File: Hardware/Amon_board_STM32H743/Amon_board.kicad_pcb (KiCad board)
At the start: 4 copper layers, 70 x 120 mm, 132 parts, among them J1 USB2.0_C_Rev, J10 GTFP08131Y2HR, J11 Conn_01x03_Male, J12 Conn_01x06_Male, J13 Conn_01x04_Male, J14 Conn_01x04_Male, J15 Conn_01x06_Male, J2 Conn_2x5 pin, J3 Switch_port, J4 XT60-F, J5 XT60-F, J6 Conn_02x04_Odd_Even, J7 Red leds, J8 White leds, J9 Conn_02x04_Odd_Even, M1 Servo_X+, M2 Servo_X-, M3 Servo_Y+, M4 Servo_Y-, Q1 BC817, Q2 BC817, SW1 SW_DPDT, SW2 SW_SPST, U1 USBLC6-2P6, U2 STM32F405RGT6-LQFP64, U3 W25Q128JVS, U4 MP2303ADN, U5 MP2303ADN, U6 MPU-6050, U7 BME280, U8 HMC5883L, Y1 25MHz

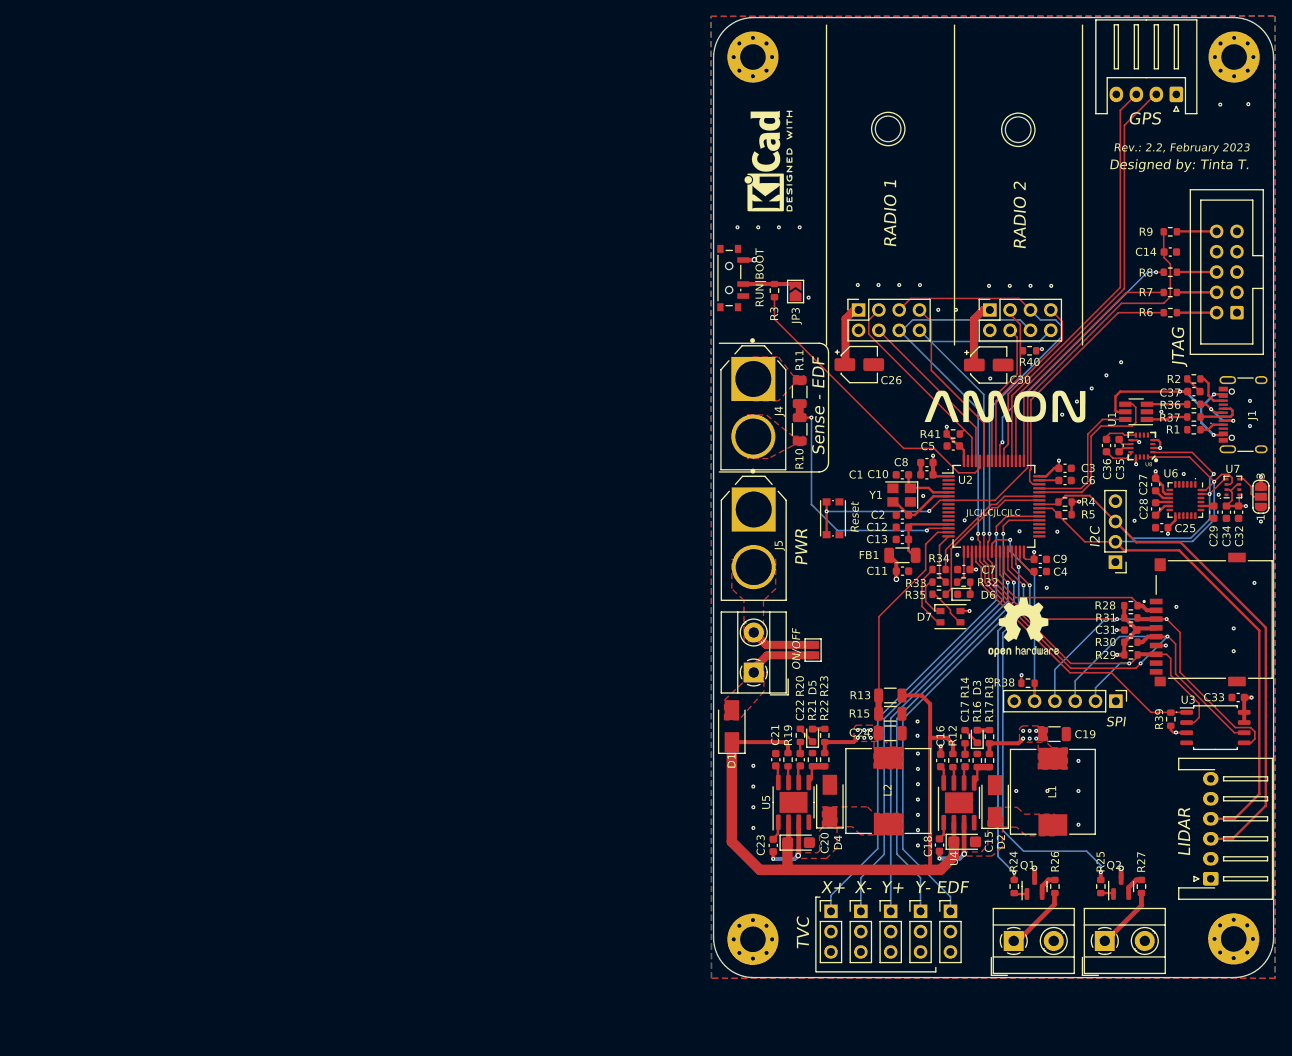
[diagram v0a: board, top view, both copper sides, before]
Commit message: Update
compas driver - untested
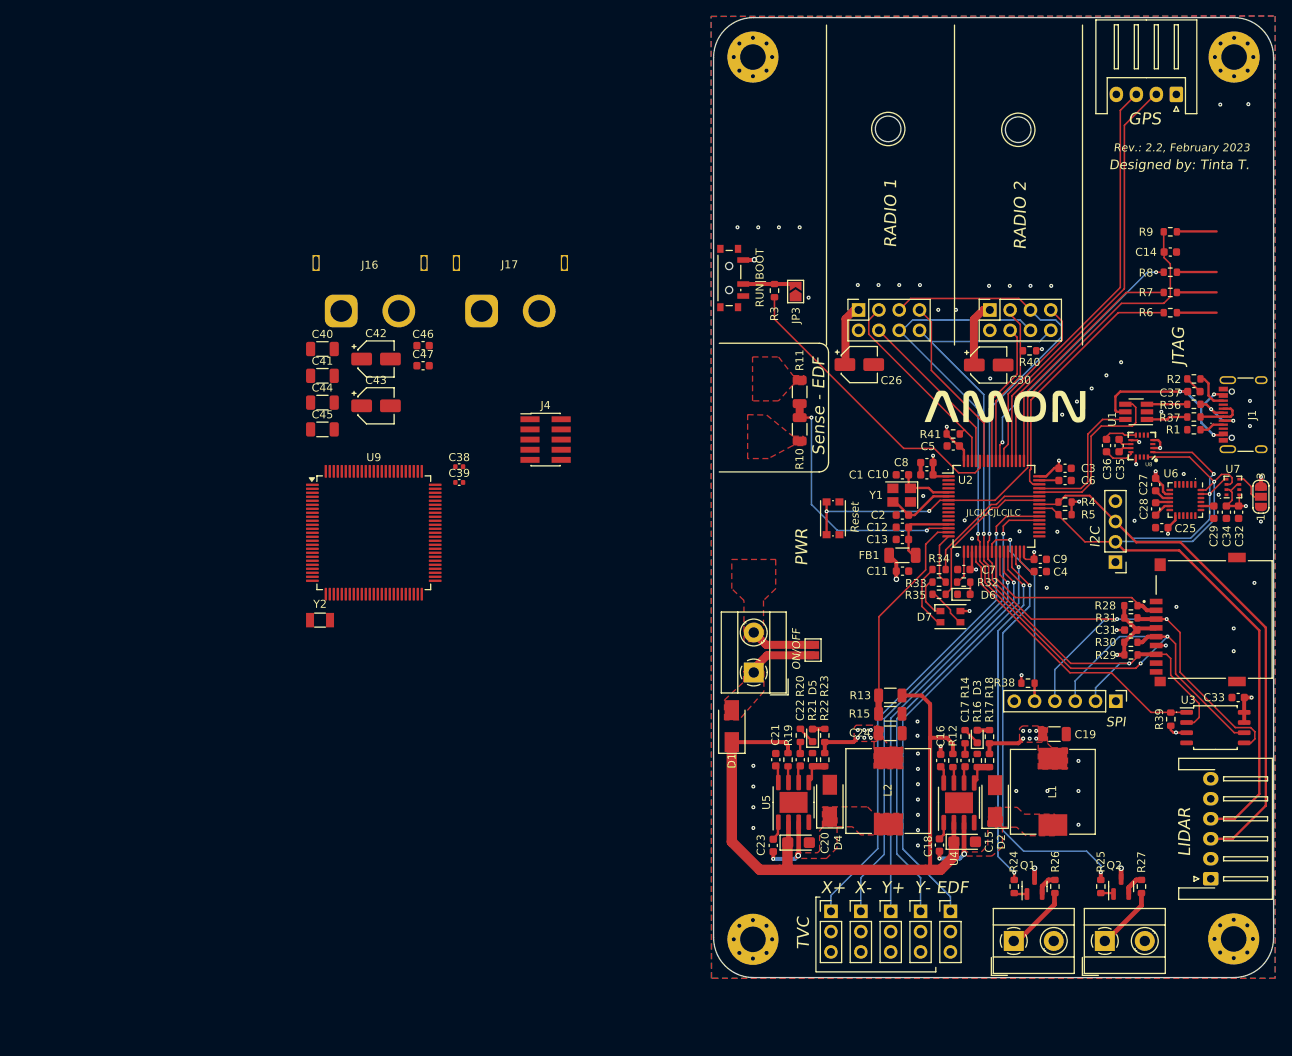
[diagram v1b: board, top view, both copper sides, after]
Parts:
- removed J2: Conn_2x5 pin, Connector_IDC:IDC-Header_2x05_P2.54mm_Vertical
- removed J5: XT60-F, XT60:AMASS_XT60-M
- removed REF**: OSHW-Logo2_9.8x8mm_SilkScreen, Symbol:OSHW-Logo2_9.8x8mm_SilkScreen
- removed REF**: KiCad-Logo2_5mm_SilkScreen, Symbol:KiCad-Logo2_5mm_SilkScreen
- added C38: 22pF, Capacitor_SMD:C_0402_1005Metric, F.Cu at (123.2, 85.1)
- added C39: 22pF, Capacitor_SMD:C_0402_1005Metric, F.Cu at (123.2, 87.1)
- added C40: 22uF, Capacitor_SMD:C_1206_3216Metric, F.Cu at (106.1, 70.4)
- added C41: 22uF, Capacitor_SMD:C_1206_3216Metric, F.Cu at (106.1, 73.8)
- added C42: 10uF, Capacitor_SMD:CP_Elec_4x5.4, F.Cu at (112.8, 71.7)
- added C43: 10uF, Capacitor_SMD:CP_Elec_4x5.4, F.Cu at (112.8, 77.5)
- added C44: 22uF, Capacitor_SMD:C_1206_3216Metric, F.Cu at (106.1, 77.1)
- added C45: 22uF, Capacitor_SMD:C_1206_3216Metric, F.Cu at (106.1, 80.5)
- added C46: 100nF, Capacitor_SMD:C_0603_1608Metric, F.Cu at (118.7, 70.0)
- added C47: 100nF, Capacitor_SMD:C_0603_1608Metric, F.Cu at (118.7, 72.5)
- added J16: XT60PW-M20, Connector_AMASS:AMASS_XT60PW-M_1x02_P7.20mm_Horizontal, F.Cu at (108.5, 65.7)
- added J17: XT60PW-M20, Connector_AMASS:AMASS_XT60PW-M_1x02_P7.20mm_Horizontal, F.Cu at (126.0, 65.7)
- added U9: STM32H743VIT6, Package_QFP:LQFP-100_14x14mm_P0.5mm, F.Cu at (112.5, 93.4)
- added Y2: 32.768kHz, Crystal:Crystal_SMD_3215-2Pin_3.2x1.5mm, F.Cu at (105.8, 104.3)
- C1, C2: value 14pF -> 15pF
- J4: value XT60-F -> HAB-VCR-010-LF; footprint XT60:AMASS_XT60-M -> Connector_PinHeader_1.27mm:PinHeader_2x05_P1.27mm_Vertical_SMD
- Y1: value 25MHz -> 48MHz
- moved J4 26.3 mm to (134.0, 81.8), turned to 0 degrees
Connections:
- C1 pad 1: /HSE_IN -> /Microcontroller/HSE_IN
- C14 pad 1: /NRST -> /Microcontroller/NRST
- C2 pad 1: /HSE_OUT -> /Microcontroller/HSE_OUT
- J4 pad 1: GND1 -> +3V3
- J4 pad 2: Net-(J4-+) -> Net-(J4-Pin_2)
- R10 pad 1: Net-(J4-+) -> Net-(J17-Pin_2)
- R11 pad 2: GND1 -> GND
- R6 pad 1: Net-(J2-Pin_2) -> Net-(J4-Pin_2)
- R6 pad 2: /SWDIO -> /Microcontroller/SWDIO
- R7 pad 1: Net-(J2-Pin_4) -> Net-(J4-Pin_4)
- R7 pad 2: /SWDCLK -> /Microcontroller/SWDCLK
- R8 pad 1: Net-(J2-Pin_6) -> Net-(J4-Pin_6)
- R8 pad 2: /SWO -> /Microcontroller/SWO
- R9 pad 1: Net-(J2-Pin_10) -> Net-(J4-Pin_10)
- R9 pad 2: /NRST -> /Microcontroller/NRST
- Y1 pad 1: /HSE_IN -> /Microcontroller/HSE_IN
- Y1 pad 3: /HSE_OUT -> /Microcontroller/HSE_OUT
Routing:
- net Net-(J4-Pin_10): track 0.00 -> 4.99 mm
- net Net-(J2-Pin_10): track 4.99 -> 0.00 mm
- net Net-(J4-Pin_6): track 0.00 -> 4.98 mm
- net Net-(J2-Pin_6): track 4.98 -> 0.00 mm
- net Net-(J4-Pin_4): track 0.00 -> 4.97 mm
- net Net-(J2-Pin_4): track 4.97 -> 0.00 mm
- net Net-(J4-Pin_2): track 0.00 -> 4.97 mm
- net Net-(J2-Pin_2): track 4.97 -> 0.00 mm
- added copper zone on F.Cu, net Net-(J17-Pin_2)
- removed copper zone on F.Cu, net GND1
- removed copper zone on F.Cu, net Net-(J4-+)

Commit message: Update: development of new PCB_v3
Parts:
- removed C1, C2: 15pF, Capacitor_SMD:C_0603_1608Metric
- removed C4, C6: 2.2uF, Capacitor_SMD:C_0603_1608Metric
- removed D1: B120-E3, Diode_SMD:D_SMA
- removed H5, H6: MountingHole, MountingHole:MountingHole_3.2mm_M3
- removed J12: Conn_01x06_Male, Connector_JST:JST_XH_S6B-XH-A-1_1x06_P2.50mm_Horizontal
- removed J6: Conn_02x04_Odd_Even, Connector_PinSocket_2.54mm:PinSocket_2x04_P2.54mm_Vertical
- removed JP3: SolderJumper_2_Open, Jumper:SolderJumper-2_P1.3mm_Open_TrianglePad1.0x1.5mm
- removed R1, R2: 5k1, Resistor_SMD:R_0603_1608Metric
- removed R3: 10k, Resistor_SMD:R_0603_1608Metric
- removed SW1: SW_DPDT, Button_Switch_SMD:SW_SPDT_PCM12
- removed SW2: SW_SPST, Button_Switch_SMD:SW_Push_1P1T_NO_CK_KMR2
- removed U1: USBLC6-2P6, Package_TO_SOT_SMD:SOT-23-6_Handsoldering
- removed U2: STM32F405RGT6-LQFP64, Package_QFP:LQFP-64_10x10mm_P0.5mm
- added C100: 100nF, Capacitor_SMD:C_0603_1608Metric, F.Cu at (104.2, 103.8)
- added C101: 10uF, Capacitor_SMD:C_1206_3216Metric, F.Cu at (115.2, 122.3)
- added C102: 10uF, Capacitor_SMD:C_1206_3216Metric, F.Cu at (98.3, 119.7)
- added C103: 10uF, Capacitor_SMD:C_1206_3216Metric, F.Cu at (80.8, 121.8)
- added C104: 10uF, Capacitor_SMD:C_1206_3216Metric, F.Cu at (80.8, 119.4)
- added C105: 10uF, Capacitor_SMD:C_1206_3216Metric, F.Cu at (80.8, 117.0)
- added C106: 10uF, Capacitor_SMD:C_1206_3216Metric, F.Cu at (98.3, 122.1)
- added C107: 10uF, Capacitor_SMD:C_1206_3216Metric, F.Cu at (98.3, 117.3)
- added C108: 10uF, Capacitor_SMD:C_1206_3216Metric, F.Cu at (115.2, 119.9)
- added C109: 10uF, Capacitor_SMD:C_1206_3216Metric, F.Cu at (115.2, 117.5)
- added C110: 4.7uF, Capacitor_SMD:C_0603_1608Metric, F.Cu at (104.2, 79.5)
- added C111: 4.7uF, Capacitor_SMD:C_0603_1608Metric, F.Cu at (117.2, 92.5)
- added C48: 0.1uF, Capacitor_SMD:C_0603_1608Metric, F.Cu at (121.5, 77.2)
- added C49: 0.1uF, Capacitor_SMD:C_0603_1608Metric, F.Cu at (125.4, 81.9)
- added C50: 10nF, Capacitor_SMD:C_0402_1005Metric, F.Cu at (102.3, 61.2)
- added C51: 10nF, Capacitor_SMD:C_0402_1005Metric, F.Cu at (82.5, 61.2)
- added C52: 33nF, Capacitor_SMD:C_0402_1005Metric, F.Cu at (102.8, 62.9)
- added C53: 33nF, Capacitor_SMD:C_0402_1005Metric, F.Cu at (83.0, 62.9)
- added C54: 1nF, Capacitor_SMD:C_0402_1005Metric, F.Cu at (110.8, 63.0)
- added C55: 1nF, Capacitor_SMD:C_0402_1005Metric, F.Cu at (91.0, 63.0)
- added C56: 1uF, Capacitor_SMD:C_0402_1005Metric, F.Cu at (104.5, 57.8)
- added C57: 1uF, Capacitor_SMD:C_0402_1005Metric, F.Cu at (84.7, 57.8)
- added C58: 22pF, Capacitor_SMD:C_0402_1005Metric, F.Cu at (112.7, 63.0)
- added C59: 22pF, Capacitor_SMD:C_0402_1005Metric, F.Cu at (92.8, 63.0)
- added C60: 22pF, Capacitor_SMD:C_0402_1005Metric, F.Cu at (111.1, 57.8)
- added C61: 22pF, Capacitor_SMD:C_0402_1005Metric, F.Cu at (91.2, 57.7)
- added C62: 2.2nF, Capacitor_SMD:C_0402_1005Metric, F.Cu at (108.4, 55.9)
- added C63: 1.5pF, Capacitor_SMD:C_0402_1005Metric, F.Cu at (106.0, 54.5)
- added C64: 2.2nF, Capacitor_SMD:C_0402_1005Metric, F.Cu at (88.5, 56.8)
- added C65: 1.5pF, Capacitor_SMD:C_0402_1005Metric, F.Cu at (86.0, 54.5)
- added C66: 1pF, Capacitor_SMD:C_0402_1005Metric, F.Cu at (105.5, 53.1)
- added C67: 1pF, Capacitor_SMD:C_0402_1005Metric, F.Cu at (85.5, 53.0)
- added C68: 4.7pF, Capacitor_SMD:C_0402_1005Metric, F.Cu at (108.4, 56.9)
- added C69: 4.7pF, Capacitor_SMD:C_0402_1005Metric, F.Cu at (88.5, 55.8)
- added C70: 220pF, Capacitor_SMD:C_0402_1005Metric, F.Cu at (102.2, 51.2)
- added C71: 220pF, Capacitor_SMD:C_0402_1005Metric, F.Cu at (82.2, 51.2)
- added C72: 0.3pF, Capacitor_SMD:C_0402_1005Metric, F.Cu at (106.0, 47.7)
- added C73: 0.3pF, Capacitor_SMD:C_0402_1005Metric, F.Cu at (86.0, 47.7)
- added C74: 1uF, Capacitor_SMD:C_0402_1005Metric, F.Cu at (102.2, 52.2)
- added C75: 1uF, Capacitor_SMD:C_0402_1005Metric, F.Cu at (82.2, 52.2)
- added C76: 1.5pF, Capacitor_SMD:C_0402_1005Metric, F.Cu at (106.0, 46.7)
- added C77: 1.5pF, Capacitor_SMD:C_0402_1005Metric, F.Cu at (86.0, 46.7)
- added C78: 1.5pF, Capacitor_SMD:C_0402_1005Metric, F.Cu at (106.0, 43.9)
- added C79: 1.5pF, Capacitor_SMD:C_0402_1005Metric, F.Cu at (86.0, 43.9)
- added C80: 1uF, Capacitor_SMD:C_0603_1608Metric, F.Cu at (128.7, 129.2)
- added C81: 1uF, Capacitor_SMD:C_0603_1608Metric, F.Cu at (127.9, 145.2)
- added C82: 0.1uF, Capacitor_SMD:C_0603_1608Metric, F.Cu at (92.1, 107.5)
- added C83: 1uF, Capacitor_SMD:C_0603_1608Metric, F.Cu at (98.3, 106.5)
- added C84: 100nF, Capacitor_SMD:C_0603_1608Metric, F.Cu at (99.3, 105.4)
- added C85: 10nF, Capacitor_SMD:C_0603_1608Metric, F.Cu at (122.0, 71.5)
- added C86: 22pF, Capacitor_SMD:C_0402_1005Metric, F.Cu at (127.4, 70.9)
- added C87: 10uF, Capacitor_Tantalum_SMD:CP_EIA-3216-10_Kemet-I, F.Cu at (122.5, 136.5)
- added C88: 100nF, Capacitor_SMD:C_0603_1608Metric, F.Cu at (112.4, 139.3)
- added C89: 3.9nF, Capacitor_SMD:C_0603_1608Metric, F.Cu at (112.4, 136.2)
- added C90: 10nF, Capacitor_SMD:C_0603_1608Metric, F.Cu at (123.0, 139.6)
- added C91: 22uF, Capacitor_SMD:C_1206_3216Metric, F.Cu at (112.0, 130.0)
- added C92: 22pF, Capacitor_SMD:C_0402_1005Metric, F.Cu at (96.6, 103.3)
- added C93: 22uF, Capacitor_SMD:C_1206_3216Metric, F.Cu at (119.9, 122.3)
- added C94: 22uF, Capacitor_SMD:C_1206_3216Metric, F.Cu at (119.9, 119.9)
- added C95: 100nF, Capacitor_SMD:C_0603_1608Metric, F.Cu at (119.2, 117.5)
- added C96: 100nF, Capacitor_SMD:C_0603_1608Metric, F.Cu at (102.3, 117.3)
- added C97: 100nF, Capacitor_SMD:C_0603_1608Metric, F.Cu at (84.8, 117.0)
- added C98: 100nF, Capacitor_SMD:C_0603_1608Metric, F.Cu at (91.9, 127.1)
- added C99: 100nF, Capacitor_SMD:C_0603_1608Metric, F.Cu at (108.8, 126.9)
- added D10: Red, LED_SMD:LED_0603_1608Metric, F.Cu at (109.3, 134.7)
- added D8: B120-E3, Diode_SMD:D_SMA, F.Cu at (83.4, 110.4)
- added D9: B120-E3, Diode_SMD:D_SMA, F.Cu at (117.6, 132.6)
- added J18: SMA Edge, Connector_Coaxial:SMA_Amphenol_132289_EdgeMount, F.Cu at (105.6, 39.5)
- added J19: SMA Edge, Connector_Coaxial:SMA_Amphenol_132289_EdgeMount, F.Cu at (85.6, 39.5)
- added J2: Conn_01x04_Pin, Connector_JST:JST_EH_S4B-EH_1x04_P2.50mm_Horizontal, F.Cu at (131.0, 137.0)
- added J5: Conn_01x04_Pin, Connector_JST:JST_EH_S4B-EH_1x04_P2.50mm_Horizontal, F.Cu at (131.0, 109.5)
- added L10: 2.4nH, Inductor_SMD:L_0402_1005Metric, F.Cu at (85.5, 45.3)
- added L11: 10uH 4A, Inductor_SMD:L_APV_APH0630, F.Cu at (117.7, 127.1)
- added L3: 8.2nH, Inductor_SMD:L_0402_1005Metric, F.Cu at (106.5, 57.8)
- added L4: 2.7nH, Inductor_SMD:L_0402_1005Metric, F.Cu at (107.0, 56.4)
- added L5: 3.9nH, Inductor_SMD:L_0402_1005Metric, F.Cu at (106.0, 56.4)
- added L6: 8.2nH, Inductor_SMD:L_0402_1005Metric, F.Cu at (86.5, 57.8)
- added L7: 2.7nH, Inductor_SMD:L_0402_1005Metric, F.Cu at (87.0, 56.3)
- added L8: 3.9nH, Inductor_SMD:L_0402_1005Metric, F.Cu at (86.0, 56.3)
- added L9: 2.4nH, Inductor_SMD:L_0402_1005Metric, F.Cu at (105.6, 45.3)
- added Q3: BC817, Package_TO_SOT_SMD:SOT-23, F.Cu at (124.2, 146.6)
- added Q6: BC817, Package_TO_SOT_SMD:SOT-23, F.Cu at (116.7, 141.8)
- added Q7: AO3401A, Package_TO_SOT_SMD:SOT-23, F.Cu at (109.7, 141.8)
- added Q8: BC817, Package_TO_SOT_SMD:SOT-23, F.Cu at (99.6, 141.5)
- added Q9: AO3401A, Package_TO_SOT_SMD:SOT-23, F.Cu at (92.6, 141.5)
- added R42: 22k, Resistor_SMD:R_0402_1005Metric, F.Cu at (102.3, 60.0)
- added R43: 22k, Resistor_SMD:R_0402_1005Metric, F.Cu at (82.5, 60.0)
- added R44: 1M, Resistor_SMD:R_0402_1005Metric, F.Cu at (109.4, 60.4)
- added R45: 1M, Resistor_SMD:R_0402_1005Metric, F.Cu at (89.5, 60.4)
- added R46: 1k, Resistor_SMD:R_0402_1005Metric, F.Cu at (108.6, 51.7)
- added R47: 1k, Resistor_SMD:R_0402_1005Metric, F.Cu at (88.5, 51.6)
- added R48: 1k, Resistor_SMD:R_0402_1005Metric, F.Cu at (108.6, 50.7)
- added R49: 20k, Resistor_SMD:R_0402_1005Metric, F.Cu at (108.6, 49.6)
- added R50: 1k, Resistor_SMD:R_0402_1005Metric, F.Cu at (88.5, 50.6)
- added R51: 20k, Resistor_SMD:R_0402_1005Metric, F.Cu at (88.5, 49.6)
- added R52: 10k, Resistor_SMD:R_0603_1608Metric, F.Cu at (93.8, 86.4)
- added R53: 5k1, Resistor_SMD:R_0603_1608Metric, F.Cu at (129.2, 63.2)
- added R54: 100k, Resistor_SMD:R_0603_1608Metric, F.Cu at (112.4, 137.8)
- added R55: 6k8, Resistor_SMD:R_0603_1608Metric, F.Cu at (109.3, 136.2)
- added R56: 10k, Resistor_SMD:R_0603_1608Metric, F.Cu at (112.4, 134.7)
- added R57: 68k, Resistor_SMD:R_0603_1608Metric, F.Cu at (112.4, 133.1)
- added R58: 1k5, Resistor_SMD:R_0603_1608Metric, F.Cu at (109.3, 133.1)
- added R59: 1k, Resistor_SMD:R_0603_1608Metric, F.Cu at (120.7, 145.7)
- added R60: 1k, Resistor_SMD:R_0603_1608Metric, F.Cu at (120.6, 147.6)
- added R63: 10k, Resistor_SMD:R_0603_1608Metric, F.Cu at (120.3, 141.1)
- added R64: 1k, Resistor_SMD:R_0603_1608Metric, F.Cu at (120.3, 142.8)
- added R65: 10k, Resistor_SMD:R_0603_1608Metric, F.Cu at (113.3, 142.8)
- added R66: 1k, Resistor_SMD:R_0603_1608Metric, F.Cu at (113.2, 141.1)
- added R67: 10k, Resistor_SMD:R_0603_1608Metric, F.Cu at (103.1, 140.8)
- added R68: 1k, Resistor_SMD:R_0603_1608Metric, F.Cu at (103.1, 142.5)
- added R69: 10k, Resistor_SMD:R_0603_1608Metric, F.Cu at (96.1, 142.5)
- added R70: 1k, Resistor_SMD:R_0603_1608Metric, F.Cu at (96.1, 140.8)
- added R71: 10k, Resistor_SMD:R_0603_1608Metric, F.Cu at (92.2, 137.4)
- added R72: 10k, Resistor_SMD:R_0603_1608Metric, F.Cu at (109.3, 137.8)
- added R73: 0R, Resistor_SMD:R_0603_1608Metric, F.Cu at (92.1, 139.0)
- added R74: 0R, Resistor_SMD:R_0603_1608Metric, F.Cu at (109.3, 139.3)
- added R75: 100k, Resistor_SMD:R_0603_1608Metric, F.Cu at (109.3, 131.6)
- added R76: 75k, Resistor_SMD:R_0603_1608Metric, F.Cu at (109.3, 130.0)
- added R77: 100k, Resistor_SMD:R_0603_1608Metric, F.Cu at (92.2, 131.3)
- added R78: 150k, Resistor_SMD:R_0603_1608Metric, F.Cu at (92.2, 129.8)
- added REF**: KiCad-Logo2_5mm_SilkScreen, Symbol:KiCad-Logo2_5mm_SilkScreen, F.Cu at (75.2, 55.5)
- added REF**: OSHW-Logo_7.5x8mm_SilkScreen, Symbol:OSHW-Logo_7.5x8mm_SilkScreen, F.Cu at (91.8, 119.3)
- added SW3: SW_SPST, Button_Switch_SMD:SW_Push_1P1T_NO_CK_KMR2, F.Cu at (89.6, 104.9)
- added U10: NRF24L01, Package_DFN_QFN:QFN-20-1EP_4x4mm_P0.5mm_EP2.5x2.5mm, F.Cu at (106.0, 61.1)
- added U11: NRF24L01, Package_DFN_QFN:QFN-20-1EP_4x4mm_P0.5mm_EP2.5x2.5mm, F.Cu at (86.1, 61.1)
- added U12: RFX2401C, RFX2401C:QFN50P300X300X60-17N, F.Cu at (105.3, 50.4)
- added U13: RFX2401C, RFX2401C:QFN50P300X300X60-17N, F.Cu at (85.2, 50.4)
- added U14: CH340G, Package_SO:SOIC-16_3.9x9.9mm_P1.27mm, F.Cu at (122.7, 66.0)
- added U15: MP2303ADN, Package_SO:SOIC-8-1EP_3.9x4.9mm_P1.27mm_EP2.62x3.51mm, F.Cu at (117.7, 137.1)
- added Y3: 16MHz, Crystal:Crystal_SMD_3225-4Pin_3.2x2.5mm, F.Cu at (111.9, 60.4)
- added Y4: 16MHz, Crystal:Crystal_SMD_3225-4Pin_3.2x2.5mm, F.Cu at (92.0, 60.3)
- added Y5: 12MHz, Crystal:Resonator_SMD_Murata_CSTxExxV-3Pin_3.0x1.1mm, F.Cu at (126.5, 72.7)
- C26: value 10uF -> 10nF; footprint Capacitor_SMD:CP_Elec_4x5.4 -> Capacitor_SMD:C_0603_1608Metric
- C30, C43: value 10uF -> 22pF; footprint Capacitor_SMD:CP_Elec_4x5.4 -> Capacitor_SMD:C_0402_1005Metric
- C42: value 10uF -> 100nF; footprint Capacitor_SMD:CP_Elec_4x5.4 -> Capacitor_SMD:C_0603_1608Metric
- J1: value USB2.0_C_Rev -> USB_C_Receptacle_USB2.0
- J3: value Switch_port -> Conn_01x04_Pin; footprint TerminalBlock_MetzConnect:TerminalBlock_MetzConnect_Type055_RT01502HDWU_1x02_P5.00mm_Horizontal -> Connector_JST:JST_EH_S4B-EH_1x04_P2.50mm_Horizontal
- J7, J8: footprint TerminalBlock_MetzConnect:TerminalBlock_MetzConnect_Type055_RT01502HDWU_1x02_P5.00mm_Horizontal -> TerminalBlock_MetzConnect:TerminalBlock_MetzConnect_Type059_RT06302HBWC_1x02_P3.50mm_Horizontal
- J9: value Conn_02x04_Odd_Even -> AUX; footprint Connector_PinSocket_2.54mm:PinSocket_2x04_P2.54mm_Vertical -> TerminalBlock_MetzConnect:TerminalBlock_MetzConnect_Type059_RT06302HBWC_1x02_P3.50mm_Horizontal
- JP1: footprint Jumper:SolderJumper-2_P1.3mm_Open_Pad1.0x1.5mm -> Jumper:SolderJumper-2_P1.3mm_Open_RoundedPad1.0x1.5mm
- L1, L2: footprint Inductor_SMD:L_10.4x10.4_H4.8 -> Inductor_SMD:L_APV_APH0630
- R36: value 22 -> 10k
- R37: value 22 -> 5k1
- moved C14 139.2 mm to (74.3, 78.6), turned to 180 degrees
- moved R9 136.7 mm to (77.3, 78.6)
- moved C33 132.1 mm to (91.7, 85.3), turned to -135 degrees
- moved U3 131.8 mm to (91.3, 80.5), turned to -135 degrees
- moved R8 131.5 mm to (81.6, 77.1), turned to 0 degrees
- moved R7 131.1 mm to (81.6, 75.5), turned to 0 degrees
- moved R6 130.7 mm to (81.6, 74.0), turned to 0 degrees
- moved R39 121.5 mm to (96.1, 80.8), turned to 45 degrees
- moved C19 120.6 mm to (77.5, 129.7), turned to -90 degrees
- moved R18 115.4 mm to (74.9, 132.8), turned to 180 degrees
- moved L1 114.2 mm to (83.2, 126.7), turned to 180 degrees
- moved D3 114.1 mm to (74.9, 134.3), turned to 180 degrees
- moved R14 112.8 mm to (74.9, 135.8), turned to 0 degrees
- moved R17 112.1 mm to (77.9, 132.8), turned to 180 degrees
- moved R16 110.8 mm to (77.9, 134.3), turned to 0 degrees
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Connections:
- net BAT_BRD_S renamed /Power/AN_BAT_BRD
- net BAT_EDF_S renamed /Power/AN_BAT_EDF
- net CS_SD renamed /Devices/CS_SD
- C26 pad 1: +3V3 -> GND
- C26 pad 2: GND -> Net-(J1-SHIELD)
- C30 pad 1: +3V3 -> GND
- C30 pad 2: GND -> Net-(U14-XI)
- C37 pad 1: VBUS -> GND
- C37 pad 2: GND -> VBUS
- C42 pad 1: +5V -> GND
- C42 pad 2: GND -> +3V3
- C43 pad 1: +3V3 -> /Microcontroller/HSE_IN
- J1 pad A6: Net-(J1-D+-PadA6) -> /Microcontroller/D+
- J1 pad A7: Net-(J1-D--PadA7) -> /Microcontroller/D-
- J1 pad B6: Net-(J1-D+-PadA6) -> /Microcontroller/D+
- J1 pad B7: Net-(J1-D--PadA7) -> /Microcontroller/D-
- J1 pad S1: unconnected-(J1-SHIELD-PadS1) -> Net-(J1-SHIELD)
- J10 pad 3: MOSI -> /Devices/MOSI
- J10 pad 5: CLK -> /Devices/CLK
- J10 pad 7: MISO -> /Devices/MISO
- J11 pad 1: PWM_EDF -> /Outputs/PWM_EDF
- J11 pad 2: +5V -> Net-(J11-Pin_2)
- J13 pad 2: TX_GPS -> /Outputs/TX_GPS
- J13 pad 3: RX_GPS -> /Outputs/RX_GPS
- J14 pad 2: SDA -> /Outputs/SDA_EXT
- J14 pad 3: SCL -> /Outputs/SCL_EXT
- J15 pad 2: MISO -> /Outputs/MISO_EXT
- J15 pad 3: CLK -> /Outputs/CLK_EXT
- J15 pad 4: MOSI -> /Outputs/MOSI_EXT
- J15 pad 5: CS_EXT -> /Outputs/CS_EXT
- J16 pad 2: /Power/VBAT+ -> Net-(D8-A)
- J3 pad 1: Net-(D1-A) -> /Outputs/CLK
- J3 pad 2: /Power/VBAT+ -> /Outputs/MOSI
- J9 pad 1: +3V3 -> Net-(J9-Pin_1)
- JP1 pad 1: Net-(D1-A) -> Net-(J11-Pin_2)
- JP1 pad 2: /Power/VBAT+ -> +5V
- M1 pad 1: PWM_Servo_X+ -> /Outputs/PWM_Servo_X+
- M1 pad 2: +5V -> +7V2
- M2 pad 1: PWM_Servo_X- -> /Outputs/PWM_Servo_X-
- M2 pad 2: +5V -> +7V2
- M3 pad 1: PWM_Servo_Y+ -> /Outputs/PWM_Servo_Y+
- M3 pad 2: +5V -> +7V2
- M4 pad 1: PWM_Servo_Y- -> /Outputs/PWM_Servo_Y-
- M4 pad 2: +5V -> +7V2
- R19 pad 1: /Power/12V -> Net-(Q9-D)
- R24 pad 2: LED_Red -> /Outputs/LED_Red
- R25 pad 2: LED_White -> /Outputs/LED_White
- R29 pad 2: MISO -> /Devices/MISO
- R30 pad 2: CLK -> /Devices/CLK
- R31 pad 2: MOSI -> /Devices/MOSI
- R32 pad 1: Brd_Led -> /Devices/BRD_Led
- R33 pad 1: RGB_Led_R -> /Devices/RGB_Led_R
- R34 pad 1: RGB_Led_G -> /Devices/RGB_Led_G
- R35 pad 1: RGB_Led_B -> /Devices/RGB_Led_B
- R36 pad 1: Net-(J1-D--PadA7) -> GND
- R36 pad 2: /IN_D- -> Net-(J1-SHIELD)
- R37 pad 1: Net-(J1-D+-PadA6) -> GND
- R37 pad 2: /IN_D+ -> Net-(J1-CC1)
- R39 pad 2: CS_Flash -> /Microcontroller/CS_F
- U3 pad 1: CS_Flash -> /Microcontroller/CS_F
- U3 pad 2: MISO -> /Microcontroller/MISO_F
- U3 pad 5: MOSI -> /Microcontroller/MOSI_F
- U3 pad 6: CLK -> /Microcontroller/SCK_F
- U6 pad 23: SCL -> /Devices/SCL
- U6 pad 24: SDA -> /Devices/SDA
- U7 pad 3: SDA -> /Devices/SDA
- U7 pad 4: SCL -> /Devices/SCL
- U8 pad 1: SCL -> /Devices/SCL
- U8 pad 15: unconnected-(U8-DRDY-Pad15) -> /Devices/DRDY
- U8 pad 16: SDA -> /Devices/SDA
- U9 pad 1: unconnected-(U9-PE2-Pad1) -> /Microcontroller/SCK_F
- U9 pad 100: unconnected-(U9-VDD-Pad100) -> +3V3
- U9 pad 11: unconnected-(U9-VDD-Pad11) -> +3V3
- U9 pad 12: unconnected-(U9-PH0-Pad12) -> /Microcontroller/HSE_IN
- U9 pad 13: unconnected-(U9-PH1-Pad13) -> /Microcontroller/HSE_OUT
- U9 pad 14: unconnected-(U9-NRST-Pad14) -> /Microcontroller/NRST
- U9 pad 2: unconnected-(U9-PE3-Pad2) -> /Microcontroller/CS_F
- U9 pad 20: unconnected-(U9-VREF+-Pad20) -> +3V3
- U9 pad 21: unconnected-(U9-VDDA-Pad21) -> +3.3VA
- U9 pad 27: unconnected-(U9-VDD-Pad27) -> +3V3
- U9 pad 4: unconnected-(U9-PE5-Pad4) -> /Microcontroller/MISO_F
- U9 pad 48: unconnected-(U9-VCAP-Pad48) -> Net-(C111-Pad1)
- U9 pad 5: unconnected-(U9-PE6-Pad5) -> /Microcontroller/MOSI_F
- U9 pad 50: unconnected-(U9-VDD-Pad50) -> +3V3
- U9 pad 6: unconnected-(U9-VBAT-Pad6) -> +3V3
- U9 pad 72: unconnected-(U9-PA13-Pad72) -> /Microcontroller/SWDIO
- U9 pad 73: unconnected-(U9-VCAP-Pad73) -> Net-(C110-Pad1)
- U9 pad 75: unconnected-(U9-VDD-Pad75) -> +3V3
- U9 pad 76: unconnected-(U9-PA14-Pad76) -> /Microcontroller/SWDCLK
- U9 pad 8: unconnected-(U9-PC14-Pad8) -> /Microcontroller/LSE_IN
- U9 pad 89: unconnected-(U9-PB3-Pad89) -> /Microcontroller/SWO
- U9 pad 9: unconnected-(U9-PC15-Pad9) -> /Microcontroller/LSE_OUT
- U9 pad 94: unconnected-(U9-BOOT0-Pad94) -> Net-(U9-BOOT0)
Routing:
- net MOSI: track 122.3 -> 0.00 mm, vias 3 -> 0
- net CLK: track 119.5 -> 0.00 mm, vias 3 -> 0
- net SCL: track 98.6 -> 0.00 mm, vias 2 -> 0
- net SDA: track 96.7 -> 0.00 mm, vias 1 -> 0
- net MISO: track 96.2 -> 0.00 mm, vias 2 -> 0
- net GND: track 18.5 -> 96.1 mm, vias 63 -> 200
- net /NRST: track 71.8 -> 0.00 mm, vias 2 -> 0
- net PWM_Servo_X+: track 62.6 -> 0.00 mm, vias 1 -> 0
- net PWM_Servo_X-: track 60.3 -> 0.00 mm, vias 1 -> 0
- net /Power/12V: track 89.9 -> 35.8 mm, vias 0 -> 9
- net PWM_EDF: track 53.6 -> 0.00 mm, vias 1 -> 0
- net TX_GPS: track 53.2 -> 0.00 mm
- net LED_White: track 53.0 -> 0.00 mm, vias 2 -> 0
- net PWM_Servo_Y-: track 52.8 -> 0.00 mm, vias 1 -> 0
- net RX_GPS: track 52.3 -> 0.00 mm
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- added copper zone on F.Cu, net +7V2
- added copper zone on In2.Cu, net +7V2
- added copper zone on F.Cu, net /Power/12V
- added copper zone on F.Cu, net Net-(D8-A)
- added copper zone on F.Cu, net Net-(D9-K)
- added copper zone on F.Cu, net Net-(J1-SHIELD)
- removed copper zone on F.Cu, net /Power/VBAT+
- removed copper zone on F.Cu, net Net-(D1-A)
- removed copper zone on F.Cu, net Net-(J17-Pin_2)
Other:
- board text added: "AUX"
- board text added: "ESC PWR"
- board text added: "MAIN"
- board text added: "O. FLOW"
- board text added: "R1"
- board text added: "R2"
- board text added: "Rev.: 3.0, May 2026"
- board text added: "TOF"
- board text removed: "CS1"
- board text removed: "CS2"
- board text removed: "EN1"
- board text removed: "EN2"
- board text removed: "IRQ1"
- board text removed: "IRQ2"
- board text removed: "LIDAR"
- board text removed: "NC"
- board text removed: "ON/OFF"
- board text removed: "PWR"
- board text removed: "RADIO 1"
- board text removed: "RADIO 2"
- board text removed: "RST"
- board text removed: "RUN|BOOT"
- board text removed: "Rev.: 2.2, February 2023"
- board text removed: "SWDIO"
- board text removed: "SWO"
- board text removed: "Sense - EDF"

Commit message: Update: finished routing of PCB_v3
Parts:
- removed R4, R5: 4k7, Resistor_SMD:R_0603_1608Metric
- removed the REF** at (91.8, 119.3)
- added R61: 10k, Resistor_SMD:R_0603_1608Metric, F.Cu at (104.2, 65.9)
- added R62: 10k, Resistor_SMD:R_0603_1608Metric, F.Cu at (85.3, 66.0)
- added R81: 4k7, Resistor_SMD:R_0603_1608Metric, F.Cu at (109.3, 107.5)
- added R82: 10k, Resistor_SMD:R_0603_1608Metric, F.Cu at (109.6, 115.1)
- added R83: 10k, Resistor_SMD:R_0603_1608Metric, F.Cu at (128.7, 115.3)
- added R84: 4k7, Resistor_SMD:R_0603_1608Metric, F.Cu at (113.8, 107.5)
- added R85: 0R, Resistor_SMD:R_0603_1608Metric, F.Cu at (120.5, 71.5)
- added REF**: OSHW-Logo_5.7x6mm_SilkScreen, Symbol:OSHW-Logo_5.7x6mm_SilkScreen, F.Cu at (115.2, 99.8)
- R38: value 10k -> 0R
- R40, R41: value 10k -> 4k7
- moved J15 62.9 mm to (120.6, 113.0), turned to -90 degrees
- moved D7 45.1 mm to (85.7, 74.0), turned to -90 degrees
- moved D6 44.9 mm to (85.8, 77.0), turned to 0 degrees
- moved J14 44.0 mm to (115.5, 110.1), turned to -90 degrees
- moved R33 40.7 mm to (89.0, 72.5), turned to 180 degrees
- moved R34 40.4 mm to (89.0, 74.0), turned to 180 degrees
- moved R35 40.3 mm to (89.0, 75.6), turned to 180 degrees
- moved R32 40.3 mm to (89.0, 77.1), turned to 180 degrees
- moved R38 31.4 mm to (118.8, 71.5), turned to -90 degrees
- moved C98 30.4 mm to (107.2, 100.9), turned to -135 degrees
- moved C99 24.7 mm to (108.4, 102.2), turned to -135 degrees
- moved R41 21.3 mm to (119.1, 81.4), turned to 90 degrees
- moved R40 20.1 mm to (119.1, 78.1), turned to -90 degrees
- moved C46 15.5 mm to (97.1, 104.3), turned to -45 degrees
- moved C25 13.9 mm to (127.0, 75.9), turned to 0 degrees
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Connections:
- net /Microcontroller/SWDCLK renamed /Microcontroller/SWCLK
- C46 pad 1: /Power/AN_BAT_EDF -> /Microcontroller/AN_BAT_EDF
- C47 pad 1: /Power/AN_BAT_BRD -> /Microcontroller/AN_BAT_MAIN
- C98 pad 1: /Power/AN_BUCK_5V -> /Microcontroller/AN_BUCK_5V
- C99 pad 1: /Power/AN_BUCK_7V2 -> /Microcontroller/AN_BUCK_7V2
- J10 pad 3: /Devices/MOSI -> /Devices/MOSI_S
- J10 pad 5: /Devices/CLK -> /Devices/CLK_S
- J10 pad 7: /Devices/MISO -> /Devices/MISO_S
- J11 pad 1: /Outputs/PWM_EDF -> /Microcontroller/PWM_EDF
- J13 pad 2: /Outputs/TX_GPS -> /Microcontroller/RX_GPS
- J13 pad 3: /Outputs/RX_GPS -> /Microcontroller/TX_GPS
- J14 pad 2: /Outputs/SDA_EXT -> /Microcontroller/SDA_EXT
- J14 pad 3: /Outputs/SCL_EXT -> /Microcontroller/SCL_EXT
- J15 pad 2: /Outputs/MISO_EXT -> /Devices/MISO_S
- J15 pad 3: /Outputs/CLK_EXT -> /Devices/CLK_S
- J15 pad 4: /Outputs/MOSI_EXT -> /Devices/MOSI_S
- J15 pad 5: /Outputs/CS_EXT -> /Microcontroller/CS_EXT
- J2 pad 1: /Outputs/SDA -> /Devices/SDA_S
- J2 pad 2: /Outputs/SCL -> /Devices/SCL_S
- J3 pad 1: /Outputs/CLK -> /Devices/CLK_S
- J3 pad 2: /Outputs/MOSI -> /Devices/MOSI_S
- J5 pad 1: /Outputs/MOT -> /Devices/MOT
- J5 pad 2: /Outputs/RST -> /Devices/RST
- J5 pad 3: /Outputs/CS -> /Devices/CS_OF
- J5 pad 4: /Outputs/MISO -> /Devices/MISO_S
- M1 pad 1: /Outputs/PWM_Servo_X+ -> /Microcontroller/PWM_Servo_X+
- M2 pad 1: /Outputs/PWM_Servo_X- -> /Microcontroller/PWM_Servo_X-
- M3 pad 1: /Outputs/PWM_Servo_Y+ -> /Microcontroller/PWM_Servo_Y+
- M4 pad 1: /Outputs/PWM_Servo_Y- -> /Microcontroller/PWM_Servo_Y-
- R10 pad 2: /Power/AN_BAT_EDF -> /Microcontroller/AN_BAT_EDF
- R11 pad 1: /Power/AN_BAT_EDF -> /Microcontroller/AN_BAT_EDF
- R13 pad 2: /Power/AN_BAT_BRD -> /Microcontroller/AN_BAT_MAIN
- R15 pad 1: /Power/AN_BAT_BRD -> /Microcontroller/AN_BAT_MAIN
- R24 pad 2: /Outputs/LED_Red -> /Microcontroller/LED_Red
- R25 pad 2: /Outputs/LED_White -> /Microcontroller/LED_White
- R29 pad 2: /Devices/MISO -> /Devices/MISO_S
- R30 pad 2: /Devices/CLK -> /Devices/CLK_S
- R31 pad 2: /Devices/MOSI -> /Devices/MOSI_S
- R38 pad 1: +3V3 -> /Microcontroller/TXD
- R38 pad 2: CS_EXT -> Net-(U14-TXD)
- R40 pad 2: CS_RF2 -> /Devices/SCL_S
- R41 pad 2: CS_RF1 -> /Devices/SDA_S
- R59 pad 2: /Outputs/AUX_port -> /Microcontroller/AUX_port
- R63 pad 2: /Power/BUCK_EN_7V2 -> /Microcontroller/BUCK_EN_7V2
- R64 pad 1: /Power/BUCK_EN_7V2 -> /Microcontroller/BUCK_EN_7V2
- R67 pad 2: /Power/BUCK_EN_5V -> /Microcontroller/BUCK_EN_5V
- R68 pad 1: /Power/BUCK_EN_5V -> /Microcontroller/BUCK_EN_5V
- R75 pad 1: /Power/AN_BUCK_7V2 -> /Microcontroller/AN_BUCK_7V2
- R76 pad 2: /Power/AN_BUCK_7V2 -> /Microcontroller/AN_BUCK_7V2
- R77 pad 1: /Power/AN_BUCK_5V -> /Microcontroller/AN_BUCK_5V
- R78 pad 2: /Power/AN_BUCK_5V -> /Microcontroller/AN_BUCK_5V
- U10 pad 2: /RF/CSN1 -> /Microcontroller/CSN1
- U10 pad 3: /RF/SCK_RF -> /Microcontroller/SCK_RF
- U10 pad 4: /RF/MOSI_RF -> /Microcontroller/MOSI_RF
- U10 pad 5: /RF/MISO_RF -> /Microcontroller/MISO_RF
- U10 pad 6: /RF/IRQ1 -> /Microcontroller/IRQ1
- U11 pad 2: /RF/CSN2 -> /Microcontroller/CSN2
- U11 pad 3: /RF/SCK_RF -> /Microcontroller/SCK_RF
- U11 pad 4: /RF/MOSI_RF -> /Microcontroller/MOSI_RF
- U11 pad 5: /RF/MISO_RF -> /Microcontroller/MISO_RF
- U11 pad 6: /RF/IRQ2 -> /Microcontroller/IRQ2
- U14 pad 2: /Microcontroller/TXD -> Net-(U14-TXD)
- U14 pad 3: /Microcontroller/RXD -> Net-(U14-RXD)
- U6 pad 23: /Devices/SCL -> /Devices/SCL_S
- U6 pad 24: /Devices/SDA -> /Devices/SDA_S
- U7 pad 3: /Devices/SDA -> /Devices/SDA_S
- U7 pad 4: /Devices/SCL -> /Devices/SCL_S
- U8 pad 1: /Devices/SCL -> /Devices/SCL_S
- U8 pad 16: /Devices/SDA -> /Devices/SDA_S
- U9 pad 15: unconnected-(U9-PC0-Pad15) -> /Microcontroller/AN_BAT_EDF
- U9 pad 16: unconnected-(U9-PC1-Pad16) -> /Microcontroller/AN_BAT_MAIN
- U9 pad 17: unconnected-(U9-PC2_C-Pad17) -> /Devices/MISO_S
- U9 pad 18: unconnected-(U9-PC3_C-Pad18) -> /Devices/MOSI_S
- U9 pad 22: unconnected-(U9-PA0-Pad22) -> /Microcontroller/PWM_Servo_X+
- U9 pad 23: unconnected-(U9-PA1-Pad23) -> /Microcontroller/PWM_Servo_X-
- U9 pad 24: unconnected-(U9-PA2-Pad24) -> /Microcontroller/PWM_Servo_Y+
- U9 pad 25: unconnected-(U9-PA3-Pad25) -> /Microcontroller/PWM_Servo_Y-
- U9 pad 28: unconnected-(U9-PA4-Pad28) -> /Microcontroller/AN_BUCK_5V
- U9 pad 29: unconnected-(U9-PA5-Pad29) -> /Microcontroller/BUCK_EN_5V
- U9 pad 30: unconnected-(U9-PA6-Pad30) -> /Microcontroller/AN_BUCK_7V2
- U9 pad 31: unconnected-(U9-PA7-Pad31) -> /Microcontroller/BUCK_EN_7V2
- U9 pad 32: unconnected-(U9-PC4-Pad32) -> /Microcontroller/LED_Red
- U9 pad 33: unconnected-(U9-PC5-Pad33) -> /Microcontroller/LED_White
- U9 pad 34: unconnected-(U9-PB0-Pad34) -> /Microcontroller/AUX_port
- U9 pad 35: unconnected-(U9-PB1-Pad35) -> /Microcontroller/PWM_EDF
- U9 pad 37: unconnected-(U9-PE7-Pad37) -> /Microcontroller/CS_EXT
- U9 pad 41: unconnected-(U9-PE11-Pad41) -> /Devices/CS_OF
- U9 pad 42: unconnected-(U9-PE12-Pad42) -> /Devices/RST
- U9 pad 43: unconnected-(U9-PE13-Pad43) -> /Devices/MOT
- U9 pad 44: unconnected-(U9-PE14-Pad44) -> /Devices/CS_SD
- U9 pad 45: unconnected-(U9-PE15-Pad45) -> /Devices/DRDY
- U9 pad 46: unconnected-(U9-PB10-Pad46) -> /Devices/SCL_S
- U9 pad 47: unconnected-(U9-PB11-Pad47) -> /Devices/SDA_S
- U9 pad 51: unconnected-(U9-PB12-Pad51) -> /Microcontroller/RXD
- U9 pad 52: unconnected-(U9-PB13-Pad52) -> /Microcontroller/TXD
- U9 pad 53: unconnected-(U9-PB14-Pad53) -> /Microcontroller/RX_GPS
- U9 pad 54: unconnected-(U9-PB15-Pad54) -> /Microcontroller/TX_GPS
- U9 pad 59: unconnected-(U9-PD12-Pad59) -> /Microcontroller/SCL_EXT
- U9 pad 60: unconnected-(U9-PD13-Pad60) -> /Microcontroller/SDA_EXT
- U9 pad 68: unconnected-(U9-PA9-Pad68) -> /Devices/CLK_S
- U9 pad 71: unconnected-(U9-PA12-Pad71) -> /Microcontroller/IRQ1
- U9 pad 78: unconnected-(U9-PC10-Pad78) -> /Microcontroller/SCK_RF
- U9 pad 79: unconnected-(U9-PC11-Pad79) -> /Microcontroller/MISO_RF
- U9 pad 80: unconnected-(U9-PC12-Pad80) -> /Microcontroller/MOSI_RF
- U9 pad 81: unconnected-(U9-PD0-Pad81) -> /Microcontroller/CSN1
- U9 pad 82: unconnected-(U9-PD1-Pad82) -> /RF/CE1
- U9 pad 86: unconnected-(U9-PD5-Pad86) -> /Microcontroller/IRQ2
- U9 pad 87: unconnected-(U9-PD6-Pad87) -> /Microcontroller/CSN2
- U9 pad 88: unconnected-(U9-PD7-Pad88) -> /RF/CE2
- U9 pad 92: unconnected-(U9-PB6-Pad92) -> /Devices/RGB_Led_R
- U9 pad 93: unconnected-(U9-PB7-Pad93) -> /Devices/RGB_Led_G
- U9 pad 95: unconnected-(U9-PB8-Pad95) -> /Devices/RGB_Led_B
- U9 pad 96: unconnected-(U9-PB9-Pad96) -> /Devices/BRD_Led
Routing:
- net /Devices/SCL_S: track 0.00 -> 99.4 mm, vias 0 -> 4
- net /Devices/SDA_S: track 0.00 -> 94.0 mm, vias 0 -> 2
- net /Devices/MOSI_S: track 0.00 -> 90.4 mm, vias 0 -> 3
- net /Devices/CLK_S: track 0.00 -> 79.2 mm, vias 0 -> 3
- net /Microcontroller/PWM_EDF: track 0.00 -> 75.4 mm, vias 0 -> 1
- net /Microcontroller/LED_Red: track 0.00 -> 75.2 mm, vias 0 -> 2
- net /Devices/MISO_S: track 0.00 -> 70.0 mm, vias 0 -> 3
- net /Microcontroller/LED_White: track 0.00 -> 68.9 mm, vias 0 -> 2
- net /Microcontroller/BUCK_EN_7V2: track 0.00 -> 67.7 mm, vias 0 -> 2
- net /Microcontroller/PWM_Servo_X+: track 0.00 -> 66.1 mm, vias 0 -> 1
- net /Microcontroller/AUX_port: track 0.00 -> 62.8 mm, vias 0 -> 2
- net /Microcontroller/PWM_Servo_X-: track 0.00 -> 62.4 mm, vias 0 -> 1
- net /Microcontroller/PWM_Servo_Y+: track 0.00 -> 59.0 mm, vias 0 -> 1
- net /Microcontroller/PWM_Servo_Y-: track 0.00 -> 55.6 mm, vias 0 -> 1
- net /Microcontroller/BUCK_EN_5V: track 0.00 -> 49.7 mm, vias 0 -> 2
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- added copper zone on B.Cu, net Net-(J1-SHIELD)
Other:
- board text added: "CS_OF"
- board text added: "MOT"
- board text added: "RST"
